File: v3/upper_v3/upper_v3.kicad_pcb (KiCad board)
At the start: 2 copper layers, 35.6 x 68.6 mm, 3 parts, among them J1 Conn_01x18, J2 Conn_01x09_Male, J3 Conn_01x09_Male

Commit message: Complete Toast PCB
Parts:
- J1: value Conn_01x18 -> Conn_01x24; footprint Connector_PinHeader_2.54mm:PinHeader_1x18_P2.54mm_Horizontal -> Connector_PinHeader_2.54mm:PinHeader_1x24_P2.54mm_Horizontal
- J2, J3: value Conn_01x09_Male -> Conn_01x05_Female; footprint Connector_PinSocket_2.54mm:PinSocket_1x09_P2.54mm_Vertical -> Connector_PinSocket_2.54mm:PinSocket_1x05_P2.54mm_Vertical
- moved J1 7.65 mm to (121.2, 127.0)
- moved J2 6.86 mm to (135.9, 68.6)
- moved J3 4.58 mm to (146.1, 127.0)
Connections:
- J1 pad 10: Net-(J1-Pad10) -> Net-(J1-Pad1)
- J1 pad 13: Net-(J1-Pad13) -> Net-(J1-Pad1)
- J1 pad 15: Net-(J1-Pad15) -> Net-(J1-Pad12)
- J1 pad 16: Net-(J1-Pad16) -> Net-(J1-Pad1)
- J1 pad 18: Net-(J1-Pad18) -> Net-(J1-Pad12)
- J1 pad 3: Net-(J1-Pad3) -> Net-(J1-Pad12)
- J1 pad 4: Net-(J1-Pad4) -> Net-(J1-Pad1)
- J1 pad 6: Net-(J1-Pad6) -> Net-(J1-Pad12)
- J1 pad 7: Net-(J1-Pad7) -> Net-(J1-Pad1)
- J1 pad 9: Net-(J1-Pad9) -> Net-(J1-Pad12)
- J2 pad 1: Net-(J1-Pad18) -> Net-(J1-Pad23)
- J2 pad 2: Net-(J1-Pad17) -> Net-(J1-Pad20)
- J2 pad 3: Net-(J1-Pad16) -> Net-(J1-Pad17)
- J2 pad 4: Net-(J1-Pad15) -> Net-(J1-Pad14)
- J2 pad 5: Net-(J1-Pad14) -> Net-(J1-Pad1)
- J3 pad 1: Net-(J1-Pad9) -> Net-(J1-Pad12)
- J3 pad 2: Net-(J1-Pad8) -> Net-(J1-Pad11)
- J3 pad 3: Net-(J1-Pad7) -> Net-(J1-Pad8)
- J3 pad 4: Net-(J1-Pad6) -> Net-(J1-Pad5)
- J3 pad 5: Net-(J1-Pad5) -> Net-(J1-Pad2)
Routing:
- net Net-(J1-Pad1): track 14.8 -> 119.5 mm
- net Net-(J1-Pad12): track 36.4 -> 117.1 mm
- net Net-(J1-Pad9): track 43.6 -> 0.00 mm
- net Net-(J1-Pad10): track 43.5 -> 0.00 mm
- net Net-(J1-Pad7): track 36.4 -> 0.00 mm
- net Net-(J1-Pad6): track 32.8 -> 0.00 mm
- net Net-(J1-Pad13): track 32.8 -> 0.00 mm
- net Net-(J1-Pad4): track 25.6 -> 0.00 mm
- net Net-(J1-Pad15): track 25.6 -> 0.00 mm
- net Net-(J1-Pad3): track 22.0 -> 0.00 mm
- net Net-(J1-Pad16): track 22.0 -> 0.00 mm
- net Net-(J1-Pad20): track 0.00 -> 21.5 mm
- net Net-(J1-Pad23): track 0.00 -> 15.8 mm
- net Net-(J1-Pad18): track 14.8 -> 0.00 mm
- net Net-(J1-Pad8): track 40.0 -> 27.9 mm
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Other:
- board size 35.6 x 68.6 mm -> 39.4 x 63.5 mm

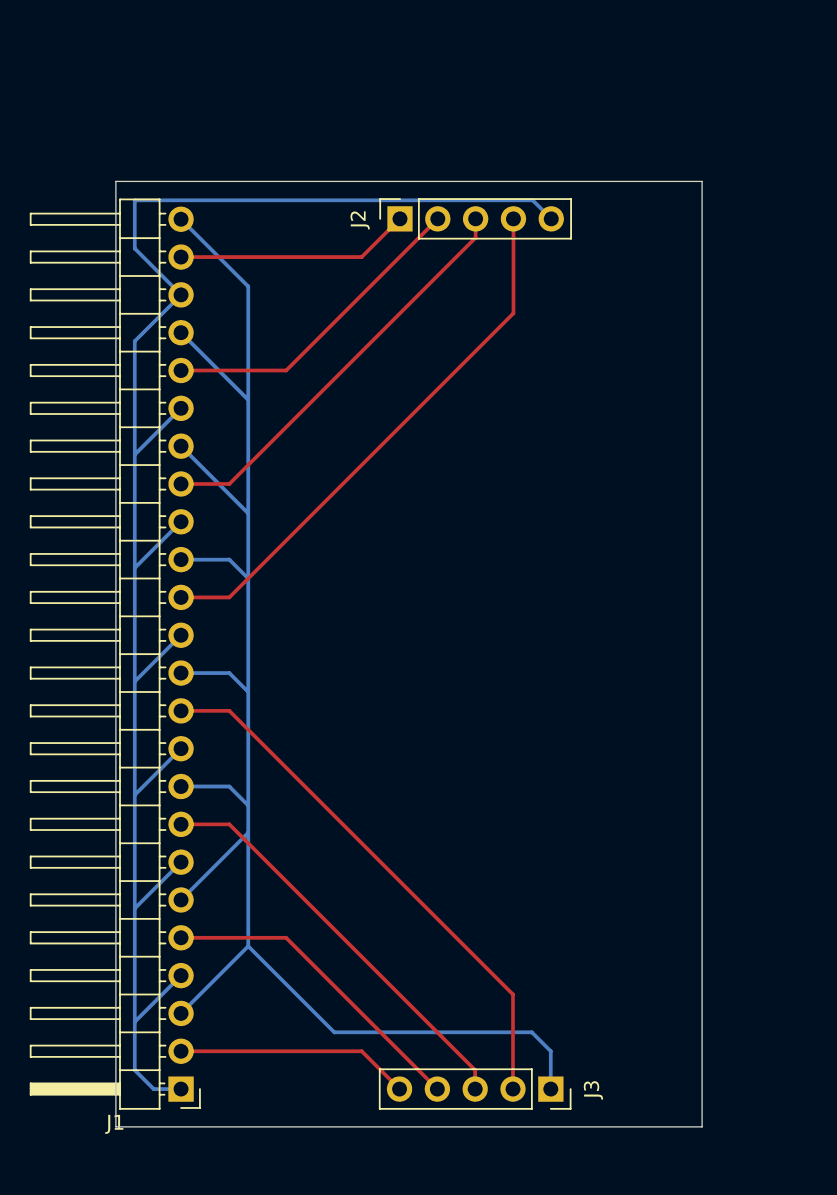
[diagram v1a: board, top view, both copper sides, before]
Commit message: Adding clear Proto-board portion for the DOME
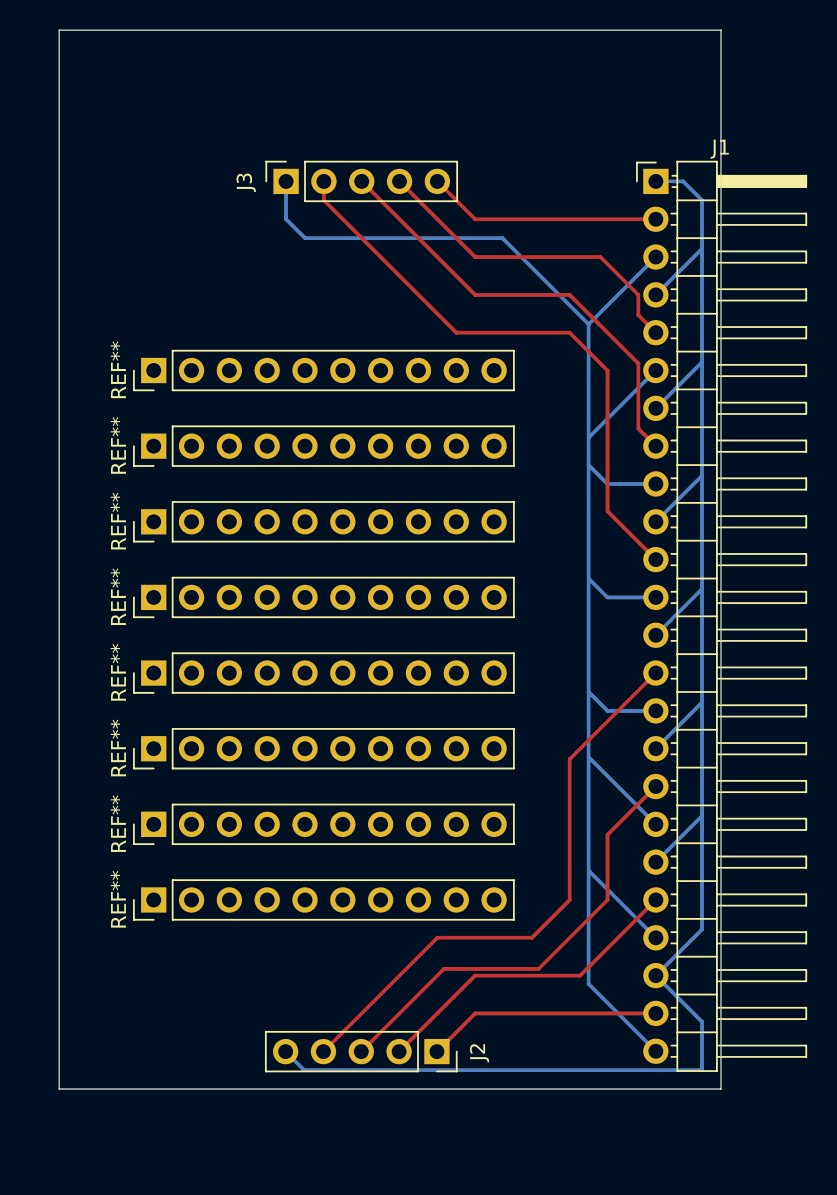
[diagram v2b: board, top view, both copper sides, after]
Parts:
- added REF**: PinHeader_1x10_P2.54mm_Vertical, Connector_PinHeader_2.54mm:PinHeader_1x10_P2.54mm_Vertical, F.Cu at (119.4, 109.2)
- added REF**: PinHeader_1x10_P2.54mm_Vertical, Connector_PinHeader_2.54mm:PinHeader_1x10_P2.54mm_Vertical, F.Cu at (119.4, 99.1)
- added REF**: PinHeader_1x10_P2.54mm_Vertical, Connector_PinHeader_2.54mm:PinHeader_1x10_P2.54mm_Vertical, F.Cu at (119.4, 104.1)
- added REF**: PinHeader_1x10_P2.54mm_Vertical, Connector_PinHeader_2.54mm:PinHeader_1x10_P2.54mm_Vertical, F.Cu at (119.4, 88.9)
- added REF**: PinHeader_1x10_P2.54mm_Vertical, Connector_PinHeader_2.54mm:PinHeader_1x10_P2.54mm_Vertical, F.Cu at (119.4, 83.8)
- added REF**: PinHeader_1x10_P2.54mm_Vertical, Connector_PinHeader_2.54mm:PinHeader_1x10_P2.54mm_Vertical, F.Cu at (119.4, 78.7)
- added REF**: PinHeader_1x10_P2.54mm_Vertical, Connector_PinHeader_2.54mm:PinHeader_1x10_P2.54mm_Vertical, F.Cu at (119.4, 114.3)
- added REF**: PinHeader_1x10_P2.54mm_Vertical, Connector_PinHeader_2.54mm:PinHeader_1x10_P2.54mm_Vertical, F.Cu at (119.4, 94.0)
- moved J1 68.8 mm to (153.1, 66.0), turned to 0 degrees
- moved J3 63.5 mm to (128.3, 66.0), turned to 90 degrees
- moved J2 56.0 mm to (138.4, 124.5), turned to -90 degrees
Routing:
- net Net-(J1-Pad11): track 36.5 -> 39.1 mm
- net Net-(J1-Pad17): track 27.9 -> 29.7 mm
- net Net-(J1-Pad14): track 36.6 -> 38.4 mm
- net Net-(J1-Pad8): track 27.9 -> 29.7 mm
- net Net-(J1-Pad5): track 21.4 -> 22.2 mm
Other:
- board size 39.4 x 63.5 mm -> 44.4 x 71.1 mm

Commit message: Rev.A Toast Design, fixing connection between 2 boards, adding 3 I/O for the DOME, creating blank proto area for testing
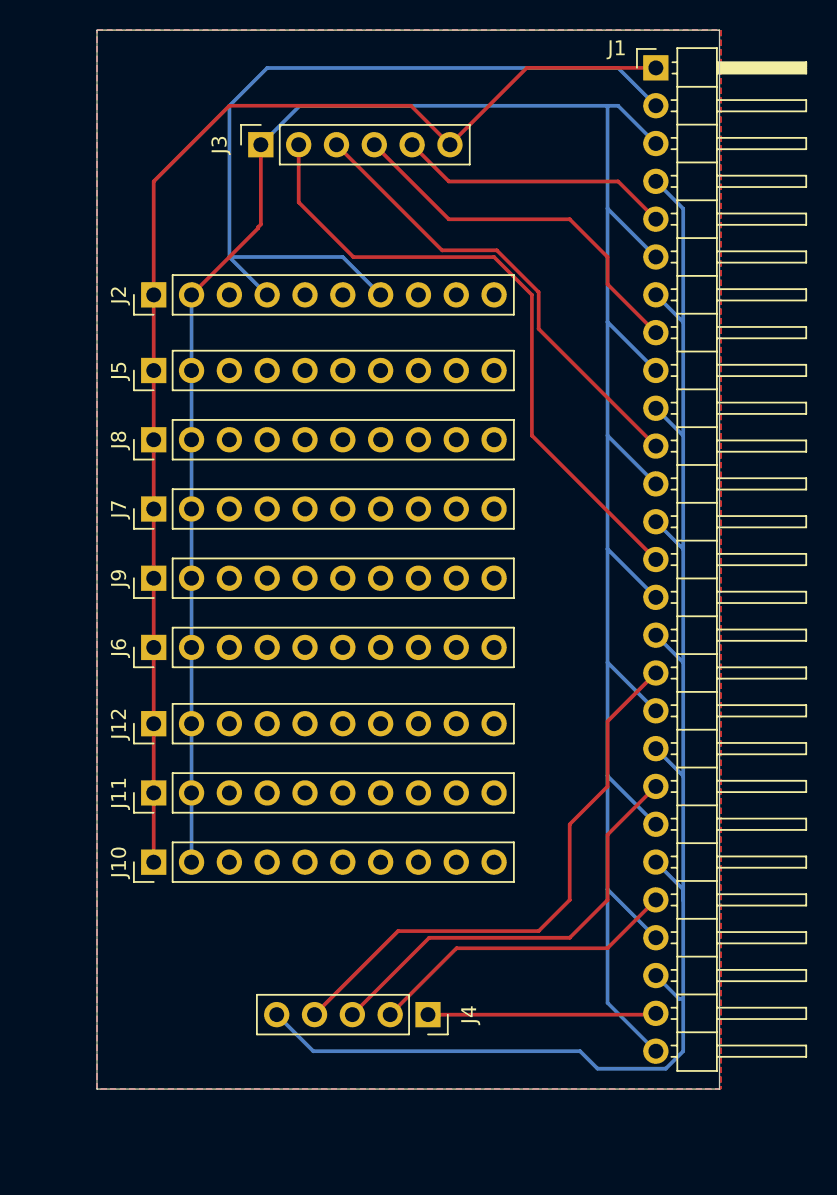
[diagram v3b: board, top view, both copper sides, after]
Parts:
- removed REF** (x8): PinHeader_1x10_P2.54mm_Vertical, Connector_PinHeader_2.54mm:PinHeader_1x10_P2.54mm_Vertical
- added J10: Conn_01x10_Male, Connector_PinHeader_2.54mm:PinHeader_1x10_P2.54mm_Vertical, F.Cu at (119.4, 111.8)
- added J11: Conn_01x10_Male, Connector_PinHeader_2.54mm:PinHeader_1x10_P2.54mm_Vertical, F.Cu at (119.4, 107.1)
- added J12: Conn_01x10_Male, Connector_PinHeader_2.54mm:PinHeader_1x10_P2.54mm_Vertical, F.Cu at (119.4, 102.5)
- added J4: Conn_01x05_Female, Connector_PinSocket_2.54mm:PinSocket_1x05_P2.54mm_Vertical, F.Cu at (137.8, 122.0)
- added J5: Conn_01x10_Male, Connector_PinHeader_2.54mm:PinHeader_1x10_P2.54mm_Vertical, F.Cu at (119.4, 78.7)
- added J6: Conn_01x10_Male, Connector_PinHeader_2.54mm:PinHeader_1x10_P2.54mm_Vertical, F.Cu at (119.4, 97.3)
- added J7: Conn_01x10_Male, Connector_PinHeader_2.54mm:PinHeader_1x10_P2.54mm_Vertical, F.Cu at (119.4, 88.0)
- added J8: Conn_01x10_Male, Connector_PinHeader_2.54mm:PinHeader_1x10_P2.54mm_Vertical, F.Cu at (119.4, 83.4)
- added J9: Conn_01x10_Male, Connector_PinHeader_2.54mm:PinHeader_1x10_P2.54mm_Vertical, F.Cu at (119.4, 92.7)
- J1: value Conn_01x24 -> Conn_01x27; footprint Connector_PinHeader_2.54mm:PinHeader_1x24_P2.54mm_Horizontal -> Connector_PinHeader_2.54mm:PinHeader_1x27_P2.54mm_Horizontal
- J2: value Conn_01x05_Female -> Conn_01x10_Male; footprint Connector_PinSocket_2.54mm:PinSocket_1x05_P2.54mm_Vertical -> Connector_PinHeader_2.54mm:PinHeader_1x10_P2.54mm_Vertical
- J3: value Conn_01x05_Female -> Conn_01x06_Female; footprint Connector_PinSocket_2.54mm:PinSocket_1x05_P2.54mm_Vertical -> Connector_PinSocket_2.54mm:PinSocket_1x06_P2.54mm_Vertical
- moved J2 54.3 mm to (119.4, 73.7), turned to 90 degrees
- moved J1 7.63 mm to (153.1, 58.4)
- moved J3 2.99 mm to (126.6, 63.6)
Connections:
- J1 pad 10: Net-(J1-Pad1) -> Net-(J1-Pad10)
- J1 pad 13: Net-(J1-Pad1) -> Net-(J1-Pad10)
- J1 pad 16: Net-(J1-Pad1) -> Net-(J1-Pad10)
- J1 pad 19: Net-(J1-Pad1) -> Net-(J1-Pad10)
- J1 pad 22: Net-(J1-Pad1) -> Net-(J1-Pad10)
- J1 pad 4: Net-(J1-Pad1) -> Net-(J1-Pad10)
- J1 pad 7: Net-(J1-Pad1) -> Net-(J1-Pad10)
- J2 pad 1: Net-(J1-Pad23) -> Net-(J1-Pad1)
- J2 pad 2: Net-(J1-Pad20) -> Net-(J1-Pad12)
- J2 pad 3: Net-(J1-Pad17) -> unconnected-(J2-Pad3)
- J2 pad 4: Net-(J1-Pad14) -> Net-(J1-Pad2)
- J2 pad 5: Net-(J1-Pad1) -> unconnected-(J2-Pad5)
- J3 pad 2: Net-(J1-Pad11) -> Net-(J1-Pad14)
- J3 pad 3: Net-(J1-Pad8) -> Net-(J1-Pad11)
- J3 pad 4: Net-(J1-Pad5) -> Net-(J1-Pad8)
- J3 pad 5: Net-(J1-Pad2) -> Net-(J1-Pad5)
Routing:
- net Net-(J1-Pad10): track 0.00 -> 107.9 mm
- net Net-(J1-Pad12): track 117.1 -> 175.7 mm
- net Net-(J1-Pad2): track 15.7 -> 55.7 mm
- net Net-(J1-Pad1): track 119.5 -> 84.8 mm
- net Net-(J1-Pad26): track 0.00 -> 15.3 mm
- net Net-(J1-Pad17): track 29.7 -> 38.0 mm
- net Net-(J1-Pad20): track 21.5 -> 29.3 mm
- net Net-(J1-Pad11): track 39.1 -> 31.3 mm
- net Net-(J1-Pad23): track 15.8 -> 21.0 mm
- net Net-(J1-Pad14): track 38.4 -> 43.3 mm
- net Net-(J1-Pad8): track 29.7 -> 25.2 mm
- net Net-(J1-Pad5): track 22.2 -> 18.4 mm
- added copper zone on B.Cu, net (none)
- added copper zone on F.Cu, net (none)
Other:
- board size 44.4 x 71.1 mm -> 41.8 x 71.1 mm
- board text added: "VDD"

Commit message: With OshPark order
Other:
- board text added: "Rev.A"
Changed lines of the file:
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@@
       (layerselection 0x00010fc_ffffffff)
       (disableapertmacros false)
-      (usegerberextensions false)
+      (usegerberextensions true)
       (usegerberattributes true)
       (usegerberadvancedattributes true)
@@
       (outputformat 1)
       (mirror false)
-      (drillshape 1)
+      (drillshape 0)
       (scaleselection 1)
-      (outputdirectory "")
+      (outputdirectory "../gerber/")
     )
   )
@@
     (property "Sheetname" "")
     (attr through_hole)
-    (fp_text reference "J4" (at 0 -2.77 90) (layer "F.SilkS")
+    (fp_text reference "J4" (at 0 12.705 90) (layer "F.SilkS")
       (effects (font (size 1 1) (thickness 0.15)))
     )
@@
   )
   (gr_rect (start 157.38 127) (end 115.57 55.88) (layer "Edge.Cuts") (width 0.05) (fill none))
+  (gr_text "Rev.A\n" (at 121.92 58.42) (layer "F.SilkS")
+    (effects (font (size 1.5 1.5) (thickness 0.3)))
+  )
   (gr_text "VDD" (at 124.46 60.96) (layer "B.Fab")
     (effects (font (size 1.5 1.5) (thickness 0.3)))
